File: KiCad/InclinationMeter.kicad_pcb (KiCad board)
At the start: 4 copper layers, 90 x 70 mm, 118 parts, among them J1 JST_PH_2.0mm_1x02, J2 USB-C, J3 Header_FFC_1.0mm_06, J4 Header_50mil_2x07, J5 Header_FFC_1.0mm_10, J6 Header_FFC_1.0mm_10, J7 Header_100mil_1x03, Q1 DMG2305UX, Q2 FS8205A, Q3 DMG2305UX, Q4 AO3400A, Q5 AO3400A, SW1 PEC11R-4215F-S0024, SW2 PEC11R-4215F-S0024, U1 DW01A, U10 SN74HC14PWR, U11 LM35DGS, U12 BME280, U2 LP5907MFX-3.3/NOPB, U3 TP4056, U4 LP5907MFX-3.3/NOPB, U5 SD6210A, U6 STM32G0B1RET6, U7 RN4871-I_RM128, U8 SN74AHCT244DBR, U9 24LC256-I_ST, Y1 32.768kHz, Y2 8MHz

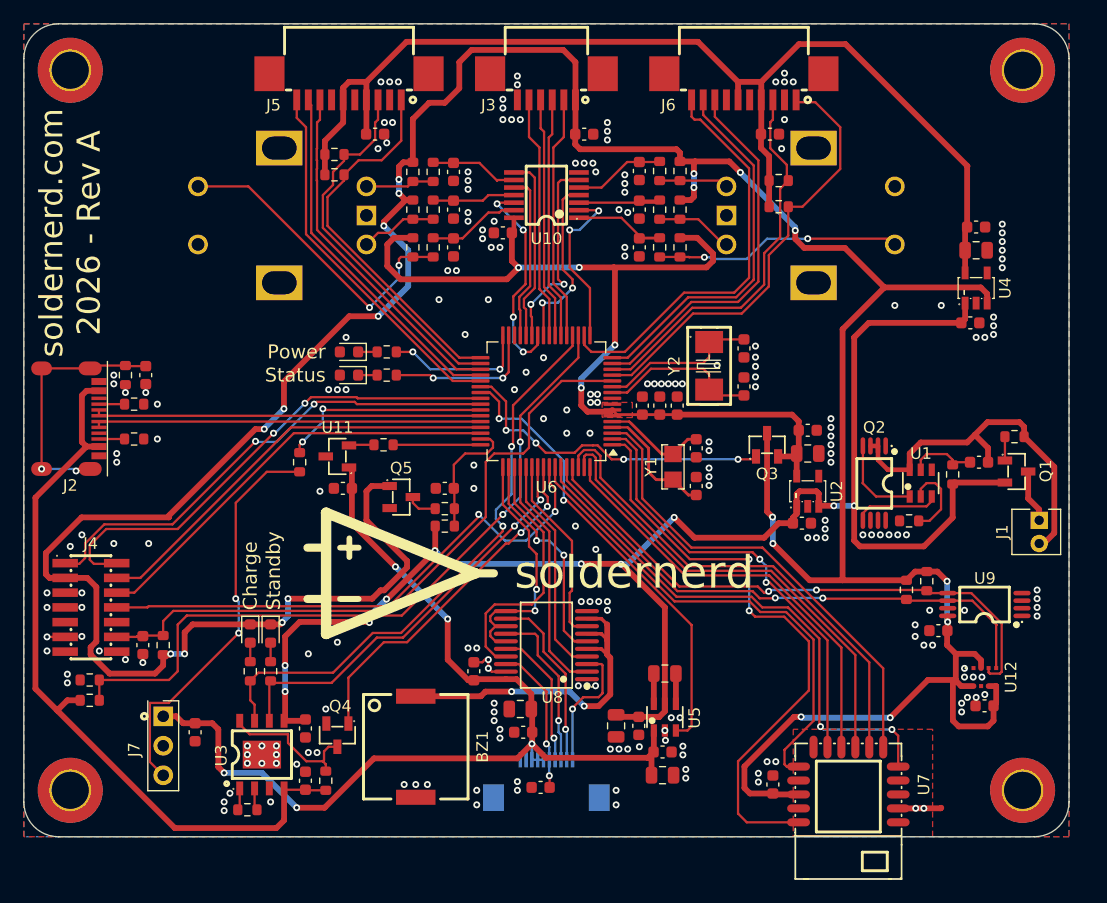
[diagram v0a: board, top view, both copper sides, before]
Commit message: JST headers fixed, no more errors, fully routed
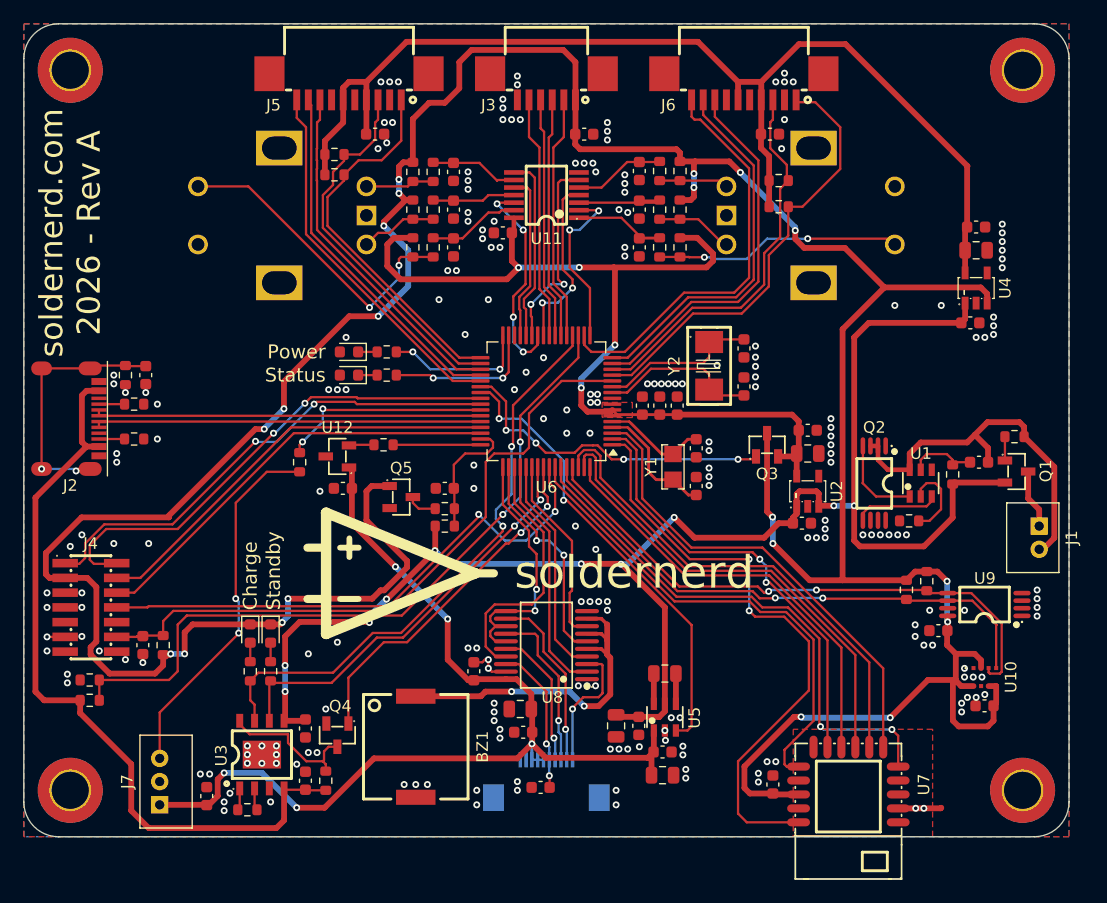
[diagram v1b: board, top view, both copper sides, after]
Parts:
- J7: value Header_100mil_1x03 -> JST_PH_2.0mm_1x03; footprint sldrnrd:Header_100mil_1x03 -> sldrnrd:JST_PH_2.0mm_1x03
- moved J7 7.63 mm to (61.7, 97.2), turned to 90 degrees
- moved C43 5.59 mm to (65.8, 96.5), turned to 90 degrees
- moved J1 0.50 mm to (137.4, 73.2)
- renumbered C42 to C34, C34 to C35, C35 to C36, C36 to C37, C41 to C38, C37 to C39, C38 to C40, C39 to C41, C40 to C42, U12 to U10, U10 to U11, U11 to U12
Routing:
- net Net-(J7-Pad3): track 34.8 -> 31.5 mm
- net 5V0: track 90.0 -> 88.3 mm
- net V_USB: track 65.5 -> 66.3 mm
- net BAT+: track 4.59 -> 5.09 mm
- net GND: vias 221 -> 223

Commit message: Capacitors changed to specific symbols, board layout not yet complete
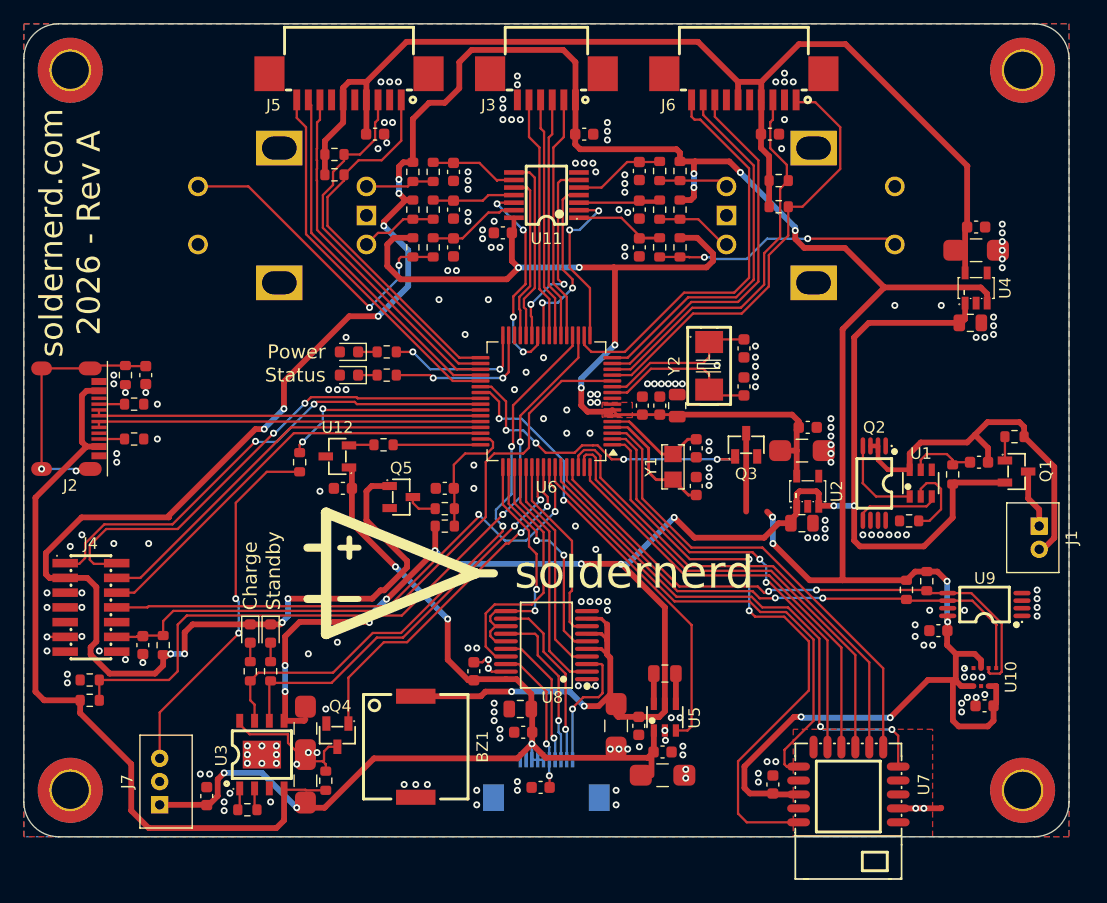
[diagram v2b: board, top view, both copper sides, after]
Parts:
- C1, C16, C6: value 1uF -> 1u; footprint sldrnrd:C_0603 -> sldrnrd:C_0805
- C10, C14, C4, C9: footprint sldrnrd:C_0805 -> sldrnrd:C_1206
- C15, C29: value 3u3 -> 2u2
- C19, C20: value 12.5p -> 12p5
- C5, C7: footprint sldrnrd:C_0603 -> sldrnrd:C_1206
- moved Q3 1.80 mm to (112.2, 66.2)
- moved C4 0.56 mm to (117.0, 66.8)
- moved C2 0.25 mm to (117.5, 64.8)

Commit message: Board layout finalized, first gerbers generated
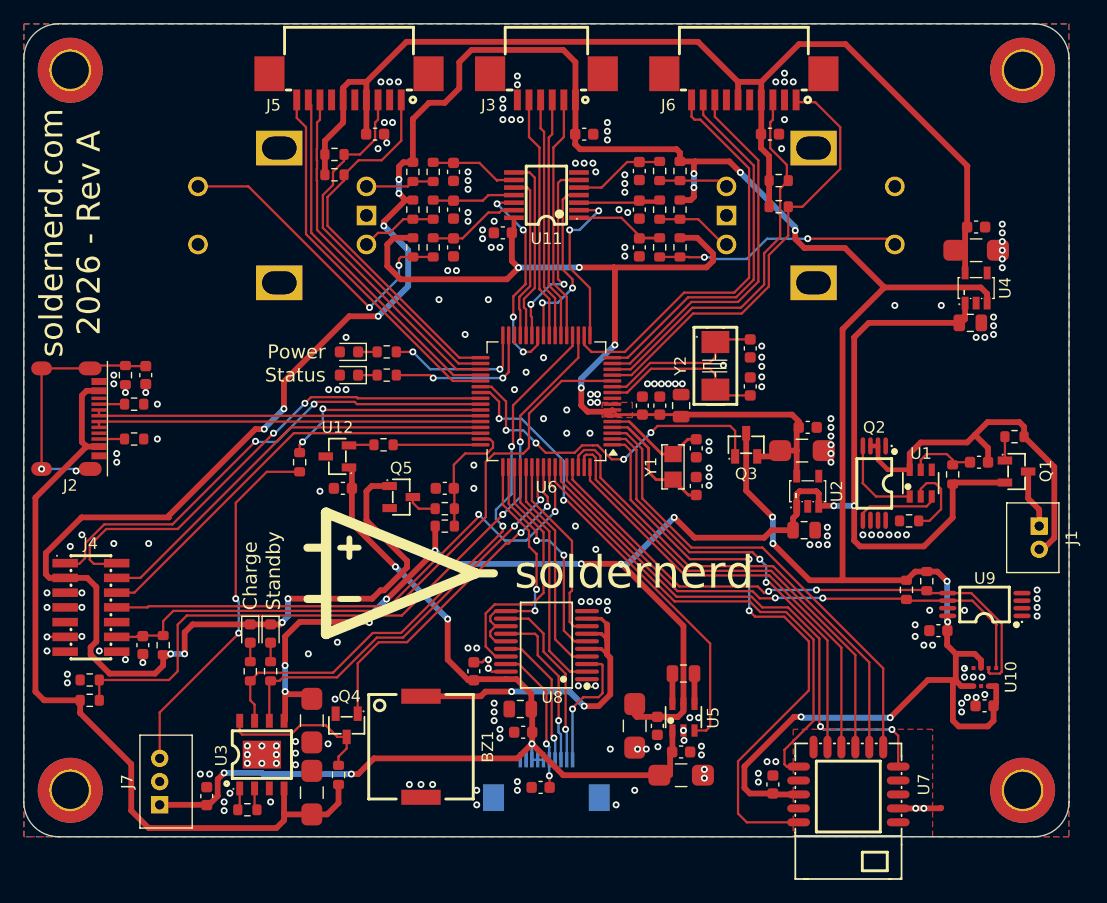
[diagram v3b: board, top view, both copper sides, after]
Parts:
- moved C10 1.60 mm to (106.6, 94.7)
- moved C11 1.60 mm to (106.6, 92.7)
- moved C12 1.60 mm to (104.5, 90.5)
- moved C14 1.60 mm to (102.6, 90.5)
- moved C15 1.60 mm to (106.8, 86.0)
- moved U5 1.60 mm to (106.8, 89.7)
- moved R5 1.21 mm to (77.1, 94.7)
- moved Q4 1.17 mm to (77.8, 90.4)
- moved C5 1.16 mm to (74.8, 96.2)
- moved C7 0.87 mm to (74.8, 90.0)
- moved C1 0.63 mm to (117.2, 73.6)
- moved C21 0.54 mm to (112.5, 61.2)
- moved C22 0.54 mm to (112.5, 58.0)
- moved Y2 0.54 mm to (109.5, 59.5)
- moved BZ1 0.45 mm to (84.2, 92.2)
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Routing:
- net V_USB: track 66.3 -> 69.5 mm
- net 3V3_STANDBY: track 80.9 -> 83.1 mm
- net VCC: track 135.8 -> 137.8 mm
- net  ~{3v3_EN}: track 28.4 -> 30.1 mm
- net 5V0: track 88.3 -> 86.9 mm
- net Net-(Q4-D): track 12.4 -> 13.8 mm
- net ~{CHARGE_EN}: track 30.7 -> 29.8 mm
- net 3V3: track 296.5 -> 297.2 mm
- net 5V_EN: track 39.6 -> 40.2 mm
- net Net-(U6-PF0): track 13.9 -> 14.4 mm
- net Net-(U6-PF1): track 13.8 -> 14.3 mm
- net GND: vias 223 -> 224

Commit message: crystal capacitors changed to correct values
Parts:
- C19, C20: value 12p5 -> 15p
- C21, C22: value 20p -> 33p
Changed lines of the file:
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@@
 			)
 		)
-		(property "Value" "12p5"
+		(property "Value" "15p"
 			(at 0 1.43 270)
 			(layer "F.Fab")
@@
 			)
 		)
-		(property "Description" "12.5pF Capacitor, 0603"
+		(property "Description" "15pF Capacitor, 0603"
 			(at 0 0 270)
 			(layer "F.Fab")
@@
 			)
 		)
-		(property "Value" "20p"
+		(property "Value" "33p"
 			(at 0 1.43 90)
 			(layer "F.Fab")
@@
 			)
 		)
-		(property "Description" "20pF Capacitor, 0603"
+		(property "Description" "33pF Capacitor, 0603"
 			(at 0 0 90)
 			(layer "F.Fab")
@@
 			)
 		)
-		(property "LCSC" "C1648"
+		(property "LCSC" "C1663"
 			(at 0 0 90)
 			(unlocked yes)
@@
 			)
 		)
-		(property "Manufacturer" "Samsung"
+		(property "Manufacturer" "Samsung Electro-Mechanics"
 			(at 0 0 90)
 			(unlocked yes)
@@
 			)
 		)
-		(property "MPN" "CL10C200JB8NNNC"
+		(property "MPN" "CL10C330JB8NNNC"
 			(at 0 0 90)
 			(unlocked yes)
@@
 			)
 		)
-		(property "Value" "20p"
+		(property "Value" "33p"
 			(at 0 1.43 270)
 			(layer "F.Fab")
@@
 			)
 		)
-		(property "Description" "20pF Capacitor, 0603"
+		(property "Description" "33pF Capacitor, 0603"
 			(at 0 0 270)
 			(layer "F.Fab")
@@
 			)
 		)
-		(property "LCSC" "C1648"
+		(property "LCSC" "C1663"
 			(at 0 0 270)
 			(unlocked yes)
@@
 			)
 		)
-		(property "Manufacturer" "Samsung"
+		(property "Manufacturer" "Samsung Electro-Mechanics"
 			(at 0 0 270)
 			(unlocked yes)
@@
 			)
 		)
-		(property "MPN" "CL10C200JB8NNNC"
+		(property "MPN" "CL10C330JB8NNNC"
 			(at 0 0 270)
 			(unlocked yes)
@@
 			)
 		)
-		(property "Value" "12p5"
+		(property "Value" "15p"
 			(at 0 1.43 90)
 			(layer "F.Fab")
@@
 			)
 		)
-		(property "Description" "12.5pF Capacitor, 0603"
+		(property "Description" "15pF Capacitor, 0603"
 			(at 0 0 90)
 			(layer "F.Fab")

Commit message: Symbols and board updated to match library
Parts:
- BZ1: value CPT-9019A -> CPT-9019A-SMT-TR
- C24, C25, C31, C33: value 10n -> C_0603
- D4: value LED_Green_0603 -> LED_Yellow_0603
- J2: value USB-C -> USB_C
- Q1, Q3: value DMG2305UX -> DMG2305UX-13
- R12, R13, R17, R20, R21, R25, R30, R9: value 68k -> R_0603
- R14, R15, R16, R22, R23, R24, R34, R5: value 33k -> R_0603
- R2, R37, R4: value 2k -> R_0603
- U12: value LM35DGS -> LM35
- U7: value RN4871-I_RM128 -> RN4871-I/RM128
- U9: value 24LC256-I_ST -> 24LC256-I/ST
- Y1: value 32.768kHz -> Q13FC1350000400
- Y2: value 8MHz -> X50328MSB2GI
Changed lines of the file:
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@@
 			)
 		)
-		(property "Value" "68k"
+		(property "Value" "R_0603"
 			(at 0 1.43 0)
 			(layer "F.Fab")
@@
 			)
 		)
-		(property "Value" "CPT-9019A"
+		(property "Value" "CPT-9019A-SMT-TR"
 			(at 0 4 270)
 			(layer "F.Fab")
@@
 			)
 		)
-		(property "Value" "68k"
+		(property "Value" "R_0603"
 			(at 0 1.43 90)
 			(layer "F.Fab")
@@
 			)
 		)
-		(property "Value" "33k"
+		(property "Value" "R_0603"
 			(at 0 1.43 270)
 			(layer "F.Fab")
@@
 			)
 		)
-		(property "Value" "RN4871-I_RM128"
+		(property "Value" "RN4871-I/RM128"
 			(at 0 7.244 180)
 			(layer "F.Fab")
@@
 			)
 		)
-		(property "Value" "32.768kHz"
+		(property "Value" "Q13FC1350000400"
 			(at 0 2.5 270)
 			(layer "F.Fab")
@@
 			)
 		)
-		(property "Value" "68k"
+		(property "Value" "R_0603"
 			(at 0 1.43 270)
 			(layer "F.Fab")
@@
 			)
 		)
-		(property "Value" "24LC256-I_ST"
+		(property "Value" "24LC256-I/ST"
 			(at 0 7.2 90)
 			(layer "F.Fab")
@@
 			)
 		)
-		(property "Value" "68k"
+		(property "Value" "R_0603"
 			(at 0 1.43 270)
 			(layer "F.Fab")
@@
 			)
 		)
-		(property "Value" "33k"
+		(property "Value" "R_0603"
 			(at 0 1.43 270)
 			(layer "F.Fab")
@@
 			)
 		)
-		(property "Value" "USB-C"
+		(property "Value" "USB_C"
 			(at 0 6 270)
 			(layer "F.Fab")
@@
 			)
 		)
-		(property "Value" "33k"
+		(property "Value" "R_0603"
 			(at 0 1.43 90)
 			(layer "F.Fab")
@@
 			)
 		)
-		(property "Value" "33k"
+		(property "Value" "R_0603"
 			(at 0 1.43 270)
 			(layer "F.Fab")
@@
 			)
 		)
-		(property "Value" "68k"
+		(property "Value" "R_0603"
 			(at 0 1.43 270)
 			(layer "F.Fab")
@@
 			)
 		)
-		(property "Value" "LM35DGS"
+		(property "Value" "LM35"
 			(at 0 4.95 0)
 			(layer "F.Fab")
@@
 			)
 		)
-		(property "Value" "2k"
+		(property "Value" "R_0603"
 			(at 0 1.43 90)
 			(layer "F.Fab")
@@
 			)
 		)
-		(property "Value" "33k"
+		(property "Value" "R_0603"
 			(at 0 1.43 90)
 			(layer "F.Fab")
@@
 			)
 		)
-		(property "Value" "10n"
+		(property "Value" "C_0603"
 			(at 0 1.43 270)
 			(layer "F.Fab")
@@
 			)
 		)
-		(property "Value" "LED_Green_0603"
+		(property "Value" "LED_Yellow_0603"
 			(at 0 1.43 180)
 			(layer "F.Fab")
@@
 			)
 		)
-		(property "Value" "33k"
+		(property "Value" "R_0603"
 			(at 0 1.43 270)
 			(layer "F.Fab")
@@
 			)
 		)
-		(property "Value" "10n"
+		(property "Value" "C_0603"
 			(at 0 1.43 270)
 			(layer "F.Fab")
@@
 			)
 		)
-		(property "Value" "10n"
+		(property "Value" "C_0603"
 			(at 0 1.43 270)
 			(layer "F.Fab")
@@
 			)
 		)
-		(property "Value" "10n"
+		(property "Value" "C_0603"
 			(at 0 1.43 270)
 			(layer "F.Fab")
@@
 			)
 		)
-		(property "Value" "68k"
+		(property "Value" "R_0603"
 			(at 0 1.43 90)
 			(layer "F.Fab")
@@
 			)
 		)
-		(property "Value" "DMG2305UX"
+		(property "Value" "DMG2305UX-13"
 			(at 0 4.95 270)
 			(layer "F.Fab")
@@
 			)
 		)
-		(property "Value" "2k"
+		(property "Value" "R_0603"
 			(at 0 1.43 180)
 			(layer "F.Fab")
@@
 			)
 		)
-		(property "Value" "2k"
+		(property "Value" "R_0603"
 			(at 0 1.43 0)
 			(layer "F.Fab")
@@
 			)
 		)
-		(property "Value" "DMG2305UX"
+		(property "Value" "DMG2305UX-13"
 			(at 0 4.95 180)
 			(layer "F.Fab")
@@
 			)
 		)
-		(property "Value" "68k"
+		(property "Value" "R_0603"
 			(at 0 1.43 180)
 			(layer "F.Fab")
@@
 			)
 		)
-		(property "Value" "8MHz"
+		(property "Value" "X50328MSB2GI"
 			(at 0 4 270)
 			(layer "F.Fab")
@@
 			)
 		)
-		(property "Value" "33k"
+		(property "Value" "R_0603"
 			(at 0 1.43 270)
 			(layer "F.Fab")
@@
 			)
 		)
-		(property "Value" "33k"
+		(property "Value" "R_0603"
 			(at 0 1.43 270)
 			(layer "F.Fab")
@@
 			)
 		)
-		(property "Value" "68k"
+		(property "Value" "R_0603"
 			(at 0 1.43 270)
 			(layer "F.Fab")

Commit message: R30 fixed as well
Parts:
- C24, C25, C31, C33: value C_0603 -> 10n
- R12, R13, R14, R15, R16, R17, R20, R21, R22, R23, R24, R25, R34, R5, R9: value R_0603 -> 33k
- R2, R37: value R_0603 -> 2k
- R26: value 1k -> 2k
- R30: value R_0603 -> 68k

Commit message: R4 changed to 2k
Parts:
- R4: value R_0603 -> 2k
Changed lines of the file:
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@@
 			)
 		)
-		(property "Value" "R_0603"
+		(property "Value" "2k"
 			(at 0 1.43 0)
 			(layer "F.Fab")
@@
 			)
 		)
-		(property "Description" "Resistor"
+		(property "Description" "2k Resistor, 0603, 1%, 75V, 100mW"
 			(at 0 0 0)
 			(layer "F.Fab")
